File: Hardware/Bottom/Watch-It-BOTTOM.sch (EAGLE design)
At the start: 31 parts, among them U1 AD5242-SO16

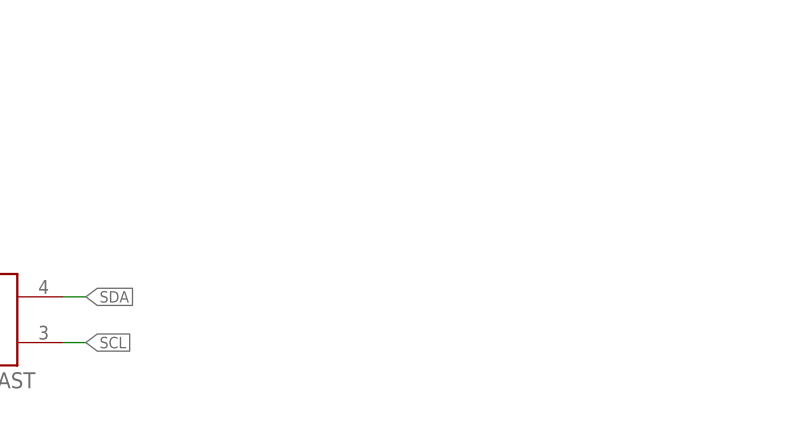
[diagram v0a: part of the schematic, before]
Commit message: rotated and added pins
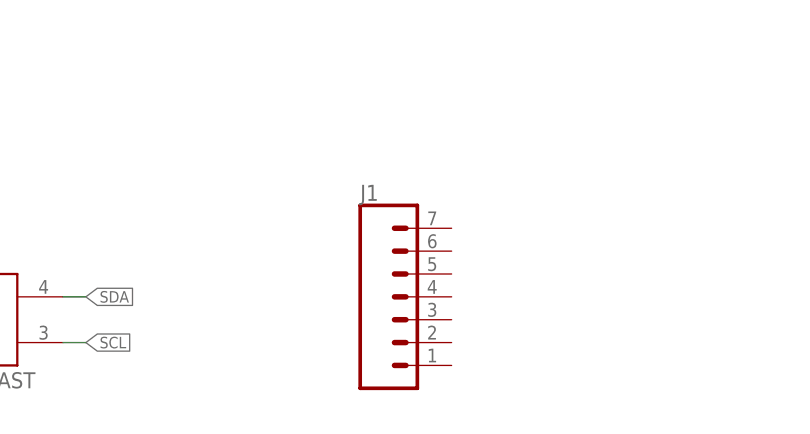
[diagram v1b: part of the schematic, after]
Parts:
- added J1: (no value), LinnesLab-Connectors:CONN_07
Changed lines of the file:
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@@
 <part name="GND2" library="LinnesLab-Symbols" deviceset="GND" device=""/>
 <part name="SUPPLY3" library="LinnesLab-Symbols" deviceset="3.3V" device=""/>
+<part name="J1" library="LinnesLab-Connectors" deviceset="CONN_07" device=""/>
 </parts>
 <sheets>
@@
 <attribute name="VALUE" x="27.94" y="43.434" size="1.778" layer="96" align="bottom-center"/>
 </instance>
+<instance part="J1" gate="G$1" x="104.14" y="33.02" smashed="yes">
+<attribute name="VALUE" x="99.06" y="23.114" size="1.778" layer="96" font="vector"/>
+<attribute name="NAME" x="99.06" y="46.228" size="1.778" layer="95" font="vector"/>
+</instance>
 </instances>

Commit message: pushing old edits
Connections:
- removed net LED.CTRL: U$4.A
- removed net PPG: C21.2, OP3G$1.OUT, U1.B2
- removed net TIA: C10.2, C15.1, OP4G$1.OUT, U1.W1
- new net A6/TIA: C10.2, C15.1, J1.5, OP4G$1.OUT, U1.W1
- new net A7/PPG: C21.2, J1.7, OP3G$1.OUT, U1.B2
- new net D29/LED.CTRL: J1.6, U$4.A
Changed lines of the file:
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@@
 </segment>
 </net>
-<net name="TIA" class="0">
+<net name="A6/TIA" class="0">
 <segment>
 <wire x1="129.54" y1="91.44" x2="124.46" y2="91.44" width="0.1524" layer="91"/>
@@
 <junction x="76.2" y="157.48"/>
 </segment>
+<segment>
+<pinref part="J1" gate="G$1" pin="5"/>
+<wire x1="109.22" y1="38.1" x2="111.76" y2="38.1" width="0.1524" layer="91"/>
+<label x="111.76" y="38.1" size="1.27" layer="95" xref="yes"/>
+</segment>
 </net>
 <net name="PD.C" class="0">
@@
 </segment>
 </net>
-<net name="LED.CTRL" class="0">
+<net name="D29/LED.CTRL" class="0">
 <segment>
 <pinref part="U$4" gate="G$1" pin="A"/>
@@
 <wire x1="226.06" y1="93.98" x2="226.06" y2="101.6" width="0.1524" layer="91"/>
 <label x="226.06" y="101.6" size="1.27" layer="95" rot="R180" xref="yes"/>
+</segment>
+<segment>
+<pinref part="J1" gate="G$1" pin="6"/>
+<wire x1="109.22" y1="40.64" x2="111.76" y2="40.64" width="0.1524" layer="91"/>
+<label x="111.76" y="40.64" size="1.27" layer="95" xref="yes"/>
 </segment>
 </net>
@@
 </segment>
 </net>
-<net name="PPG" class="0">
+<net name="A7/PPG" class="0">
 <segment>
 <wire x1="157.48" y1="91.44" x2="160.02" y2="91.44" width="0.1524" layer="91"/>
@@
 <label x="215.9" y="149.86" size="1.27" layer="95" xref="yes"/>
 </segment>
-</net>
+<segment>
+<pinref part="J1" gate="G$1" pin="7"/>
+<wire x1="109.22" y1="43.18" x2="111.76" y2="43.18" width="0.1524" layer="91"/>
+<label x="111.76" y="43.18" size="1.27" layer="95" xref="yes"/>
+</segment>
+</net>
